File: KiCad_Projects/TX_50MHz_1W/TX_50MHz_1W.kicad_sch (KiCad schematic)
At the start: 38 parts, among them J1 AIL Stick, J10 I2C Exp / OLED, J11 ANT, J2 ELE Stick, J3 THR Stick, J4 RUD Stick, J5 AUX5, J6 AUX6, J7 AUX7, J8 V_BATT In (XT30), J9 5V Logic In, Q1 RD01MUS2 (1W PA), U1 ESP32-S3-WROOM-1-N16R8, U2 Si5351A-B-GT, U3 BGS12PL6 (T/R SW), U4 SPF5043Z (LNA), U5 LT5560 (Mixer), U6 ADS1115IDGSR (0x48), U7 ADS1115IDGSR (0x49), U8 SH1106 1.3in OLED, Y1 26.000MHz

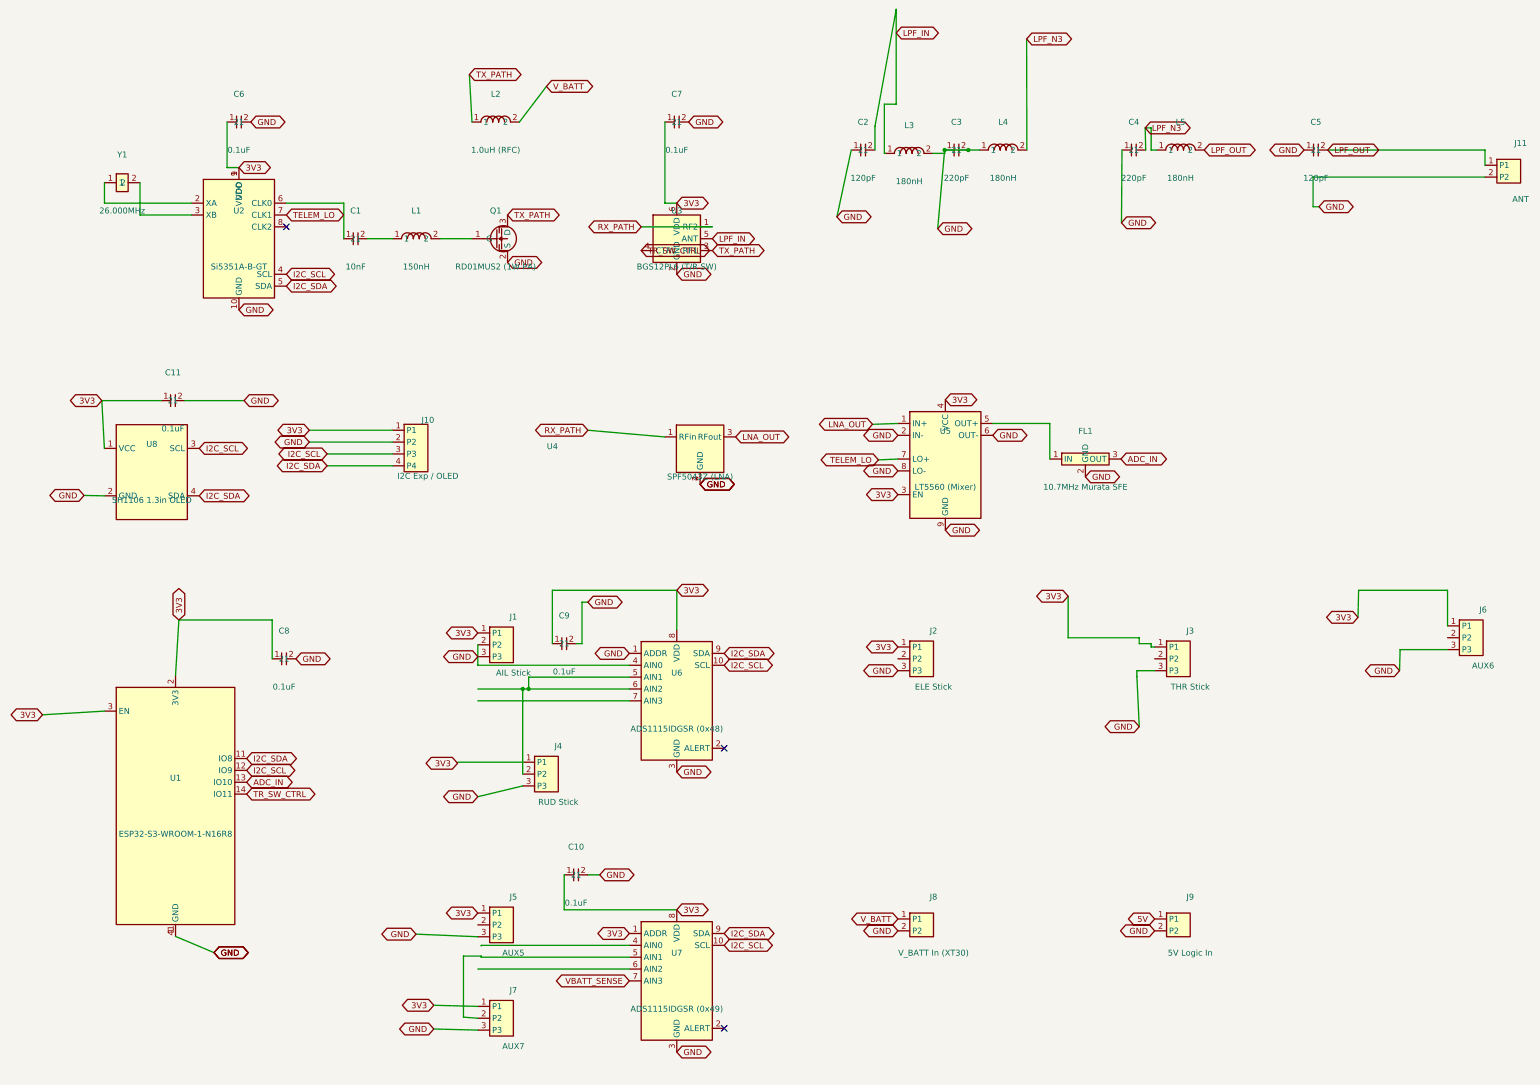
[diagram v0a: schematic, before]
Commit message: Grid-align symbols, wire the RF chain directly, use power symbols
Three related cosmetic/hygiene passes across both RX and TX schematics,
each verified with kicad-cli (netlist net-membership diff + ERC) to
confirm zero unintended connectivity change:

1. Grid alignment: every symbol placement had a small sub-grid
   fractional offset (not a multiple of the standard 1.27mm/50mil
   KiCad grid), making it impossible to snap new wires onto existing
   pins. Snapped every symbol to the nearest grid point and moved
   everything rigidly attached to it (labels, wire endpoints,
   junctions, no-connect markers) by the same delta.

2. Filter/amplifier direct wiring: the LNA -> mixer -> filter RF
   signal chain (SPF5043Z -> LT5560 -> 10.7MHz filter) used net
   labels to bridge components sitting a few centimeters apart on
   the same row. Replaced the label pairs with direct wires on both
   boards.

3. Power symbols: GND/3V3/5V/V_BATT were universally represented as
   text-shaped net labels (46-66% of all labels in each file) instead
   of KiCad's dedicated power symbols. Added power:GND/3V3/5V_RAIL/
   V_BATT/5V library symbols (GND copied byte-for-byte from KiCad's
   own power.kicad_sym; others follow the same template under
   project-specific names) and replaced every power-rail label with
   one, wired at the same point. This is also what real power symbols
   are for: ERC's "is this rail driven" check only recognizes them,
   not text labels.

The power symbol pass incidentally surfaced and fixed two pin
connections (TX: U7/C10's VDD net, and J4 pin 1) that were floating
by a fraction of a millimeter in the prior schematic - invisible at
any normal zoom, but not actually connected. Confirmed via netlist
diff that this was the only real connectivity change in either file;
everything else matches the prior net membership exactly.

Co-Authored-By: Claude Sonnet 5 <noreply@anthropic.com>
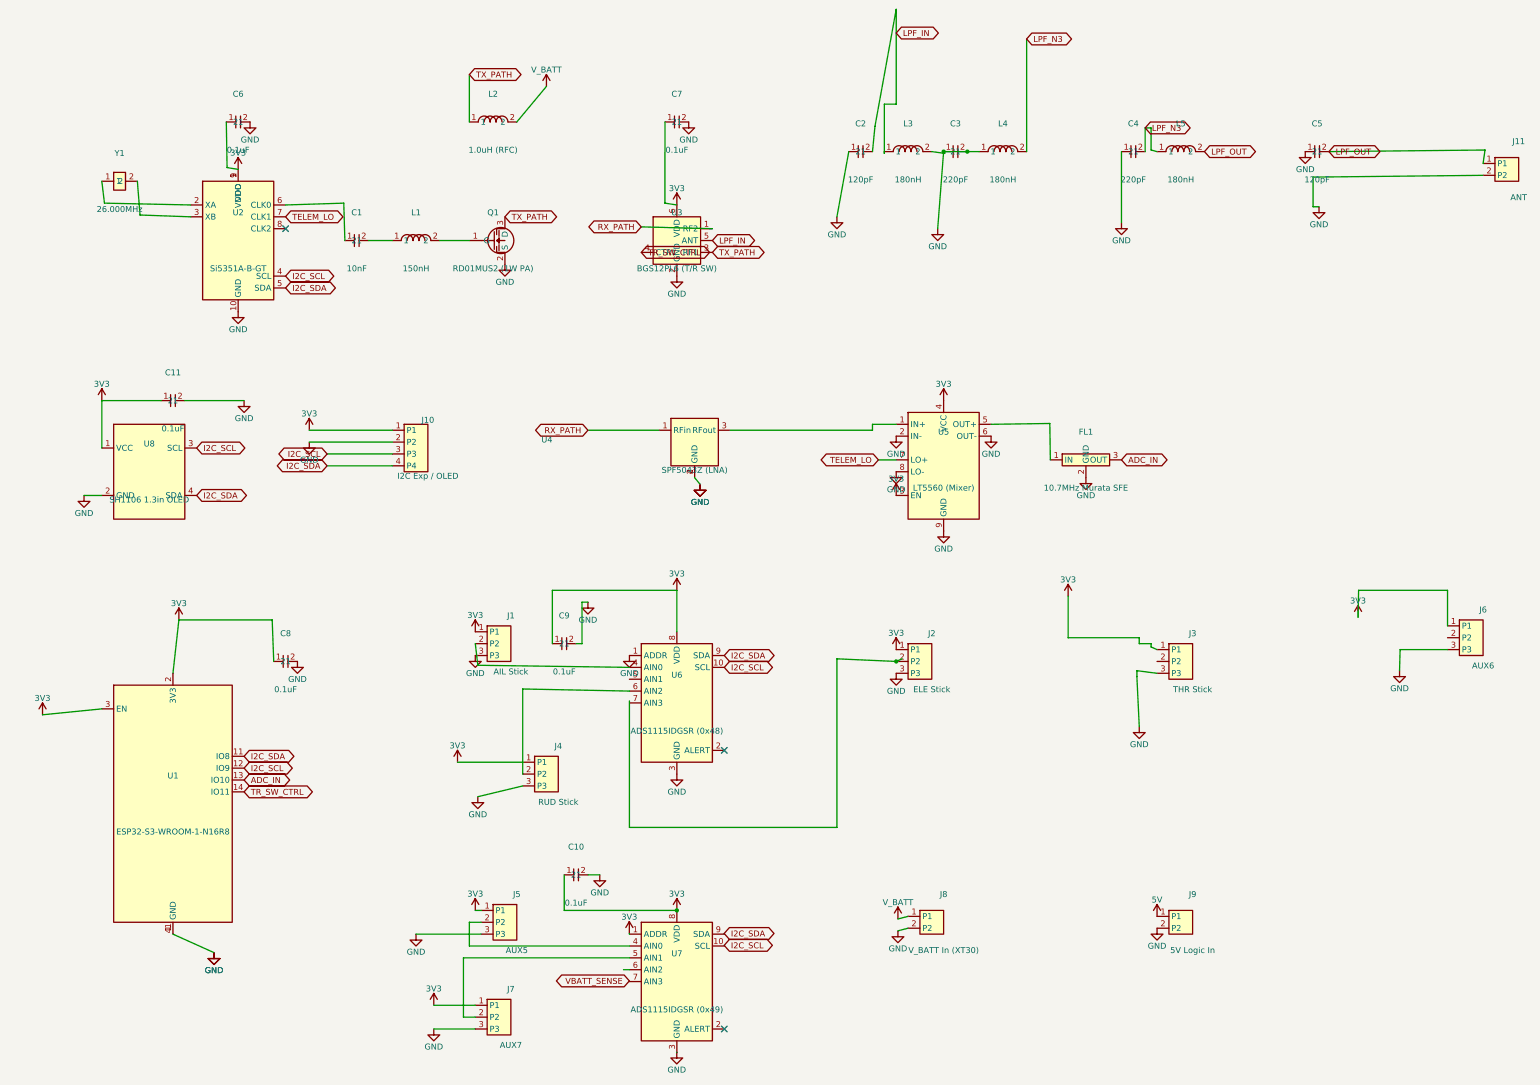
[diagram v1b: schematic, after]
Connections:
- net 3V3: now also J4.1 (P1)
- net GND: no longer J1.2 (P2), U6.4 (AIN0)
- net at U7.4 (AIN0): now also J5.2 (P2)
- net at J4.2 (P2), U6.6 (AIN2): no longer U6.5 (AIN1)
- net LNA_OUT: no longer names the net of U4.3 (RFout), U5.1 (IN+)
- new net: J1.2 (P2), U6.4 (AIN0)
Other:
- moved on the sheet: C2, C8, J1, J11, J2, J3, J5, J7, J8, J9, L2, Q1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

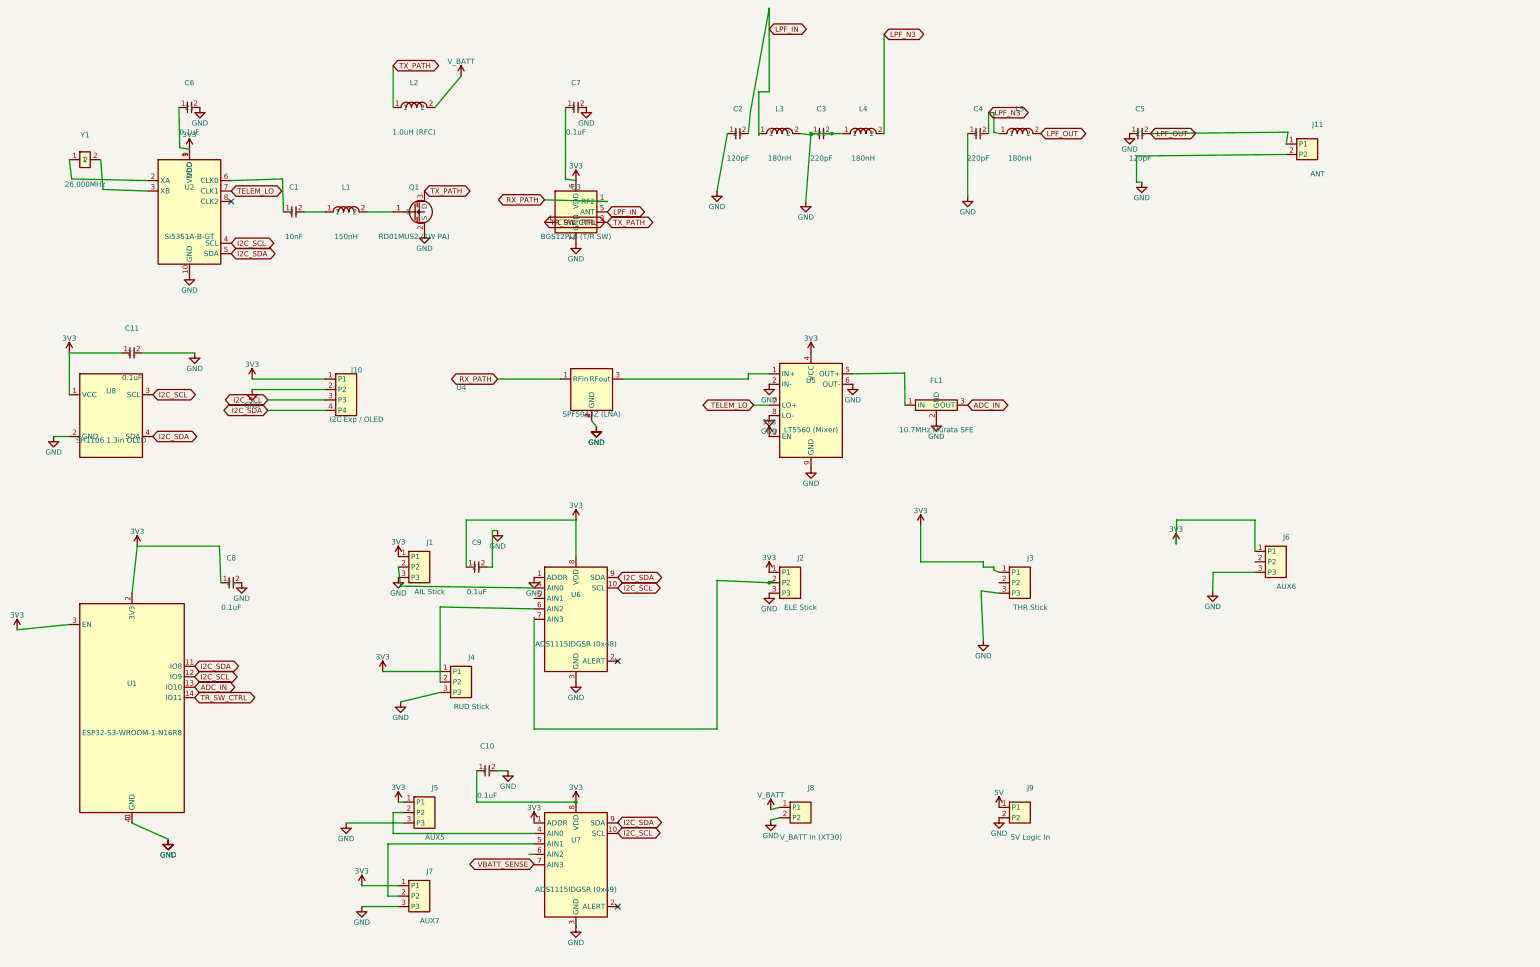
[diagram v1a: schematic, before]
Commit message: Update TX schematic/PCB and Kraft6M library (in-progress KiCad edits)
These files were modified outside this session (likely a parallel
KiCad GUI session on TX while RX work was in progress this
conversation) and are being committed as-is alongside the RX changes.
Includes a new TX_50MHz_1W.kicad_pcb. ERC sanity-checked clean load
before committing; content not otherwise reviewed by Claude.

Co-Authored-By: Claude Sonnet 5 <noreply@anthropic.com>
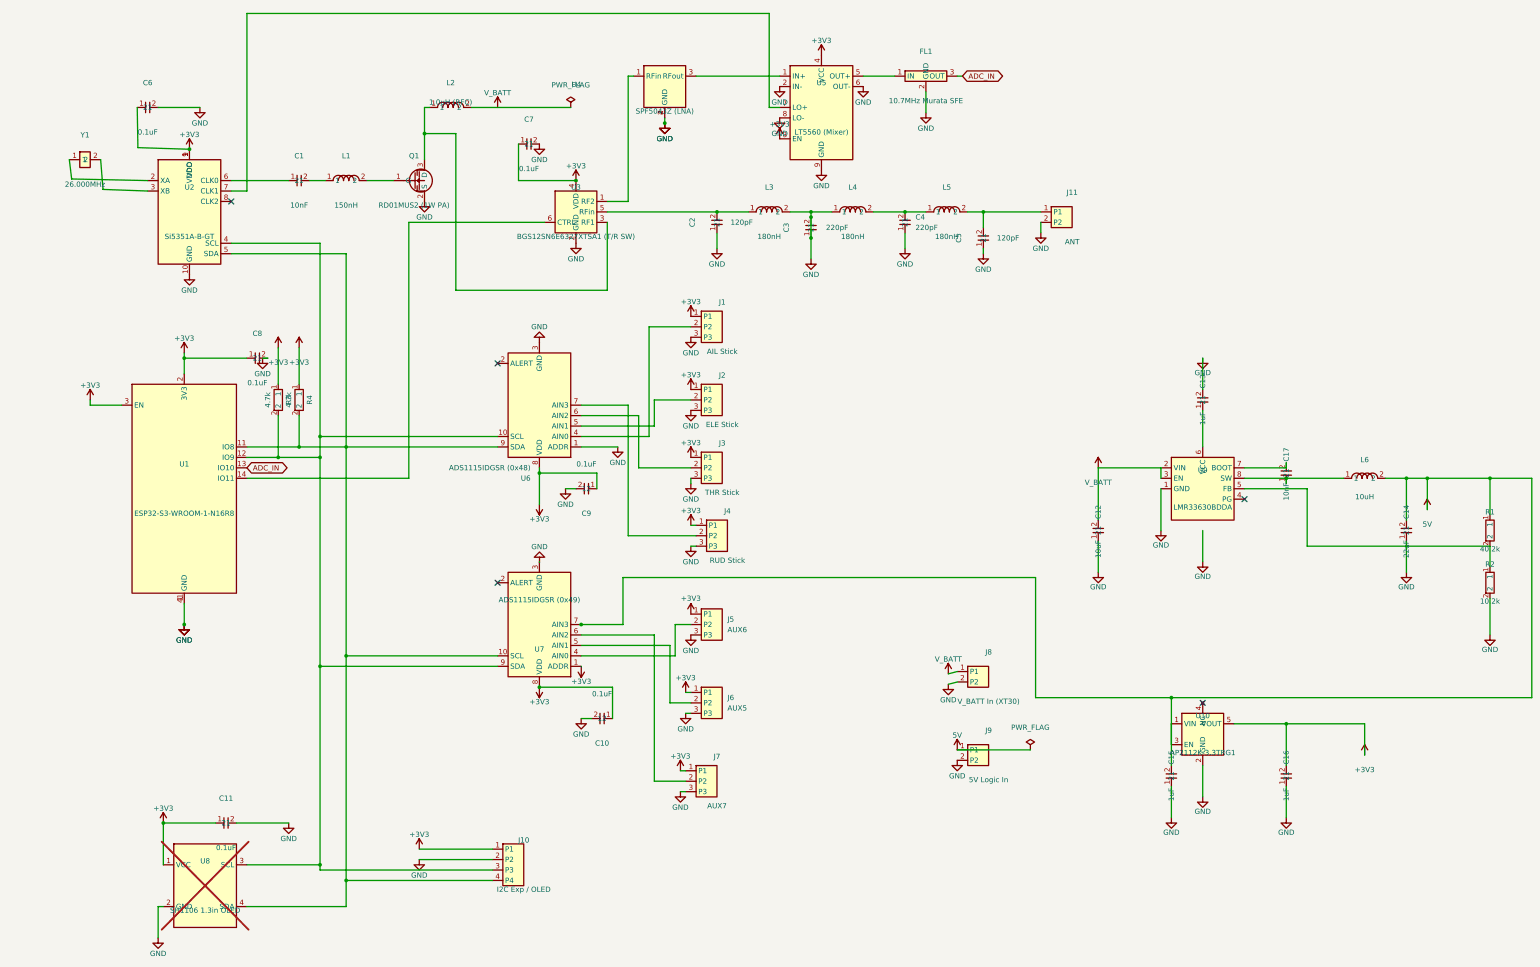
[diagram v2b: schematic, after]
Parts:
- added C12: 10uF, Capacitor_SMD:C_0805_2012Metric, symbol Kraft6M:C_10uF_0805
- added C13, C15, C16: 1uF, Capacitor_SMD:C_0603_1608Metric, symbol Kraft6M:C_1uF_0603
- added C14: 22uF, Capacitor_SMD:C_0805_2012Metric, symbol Kraft6M:C_22uF_0805
- added C17: 10nF, Capacitor_SMD:C_0603_1608Metric, symbol Kraft6M:C_10nF_0603
- added L6: 10uH, Inductor_SMD:L_0805_2012Metric, symbol Kraft6M:L_10uH_0805
- added R1: 40.2k, Resistor_SMD:R_0603_1608Metric, symbol Kraft6M:R_40.2k_0603
- added R2: 10.2k, Resistor_SMD:R_0603_1608Metric, symbol Kraft6M:R_10.2k_0603
- added R3, R4: 4.7k, Resistor_SMD:R_0603_1608Metric, symbol Kraft6M:R_4.7k_0603
- added U10: AP2112K-3.3TRG1, Package_TO_SOT_SMD:SOT-23-5, symbol Kraft6M:AP2112K-3.3
- added U9: LMR33630BDDA, Package_SO:Texas_HSOP-8-1EP_3.9x4.9mm_P1.27mm_ThermalVias, symbol Kraft6M:LMR33630
- FL1: footprint Filter:Ceramic_Filter_Murata_SFE -> Crystal:Resonator_SMD_Murata_SFECV-3Pin_6.9x2.9mm
- U1: footprint RF_Module:ESP32-S3-WROOM-1-N16R8 -> RF_Module:ESP32-S3-WROOM-1
- U3: value BGS12PL6 (T/R SW) -> BGS12SN6E6327XTSA1 (T/R SW); footprint Package_SON:TSLP-6-4_0.7x1.1mm_P0.4mm -> Package_LGA:Infineon_PG-TSNP-6-10_0.7x1.1mm_0.7x1.1mm_P0.4mm
- U5: footprint Package_SON:DFN-8-1EP_2x2mm_P0.5mm_EP0.6x1.0mm -> Package_DFN_QFN:DFN-8-1EP_2x2mm_P0.5mm_EP0.6x1.2mm
- U6, U7: footprint Package_SO:VSSOP-10_3x3mm_P0.5mm -> Package_SO:HVSSOP-10-1EP_3x3mm_P0.5mm_EP1.83x1.89mm
- U8: footprint Display:OLED-13-128x64 -> Connector_JST:JST_XH_B4B-XH-A_1x04_P2.50mm_Vertical; now not fitted
- renumbered J6 to J5, J5 to J6
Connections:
- net VBATT_SENSE is gone; now on net 5V: U7.7 (AIN3)
- net 5V: now also C14.2, C15.2, L6.2, R1.1, U10.1 (VIN), U10.3 (EN)
- net GND: now also C12.1, C13.2, C14.1, C15.1, C16.1, R2.2, U10.2 (GND), U9.1 (GND), U9.9 (GND)
- net V_BATT: now also C12.2, U9.2 (VIN), U9.3 (EN)
- net at J2.2 (P2): now also U6.5 (AIN1)
- net at J5.2 (P2): now also U7.4 (AIN0)
- net at J6.2 (P2): now also U7.5 (AIN1); no longer U7.4 (AIN0)
- net at J7.2 (P2): now also U7.6 (AIN2); no longer U7.5 (AIN1)
- net at U6.6 (AIN2): now also J3.2 (P2); no longer J4.2 (P2)
- net at U6.7 (AIN3): now also J4.2 (P2)
- net 3V3 renamed +3V3
- net +3V3: now also U3.4 (VDD), C16.2, R3.1, R4.1, U10.5 (VOUT); no longer U3.6 (VDD)
- net I2C_SCL: no longer names the net of J10.3 (P3), U1.12 (IO9), U2.4 (SCL), U6.10 (SCL), U8.3 (SCL)
- net I2C_SCL: now also U7.9 (SDA), R3.2; no longer U7.10 (SCL)
- net I2C_SDA: no longer names the net of J10.4 (P4), U1.11 (IO8), U2.5 (SDA), U6.9 (SDA), U8.4 (SDA)
- net I2C_SDA: now also U7.10 (SCL), R4.2; no longer U7.9 (SDA)
- net LPF_IN: no longer names the net of C2.2, L3.1, U3.5 (RFin)
- net LPF_N3: no longer names the net of C4.2, L4.2, L5.1
- net LPF_OUT: no longer names the net of C5.2, J11.1 (P1), L5.2
- net RX_PATH: no longer names the net of U3.1 (RF2), U4.1 (RFin)
- net TELEM_LO: no longer names the net of U2.7 (CLK1), U5.7 (LO+)
- net TR_SW_CTRL: no longer names the net of U1.14 (IO11)
- net TR_SW_CTRL: now also U3.6 (CTRL); no longer U3.4 (CTRL)
- net TX_PATH: no longer names the net of L2.1, Q1.3 (D), U3.3 (RF1)
- new net: R1.2, R2.1, U9.5 (FB)
- new net: C13.1, U9.6 (VCC)
- new net: C17.2, U9.7 (BOOT)
- new net: C17.1, L6.1, U9.8 (SW)
- no-connect marks 3 -> 5
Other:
- moved on the sheet: C1, C10, C11, C2, C3, C4, C5, C6, C7, C8, C9, FL1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

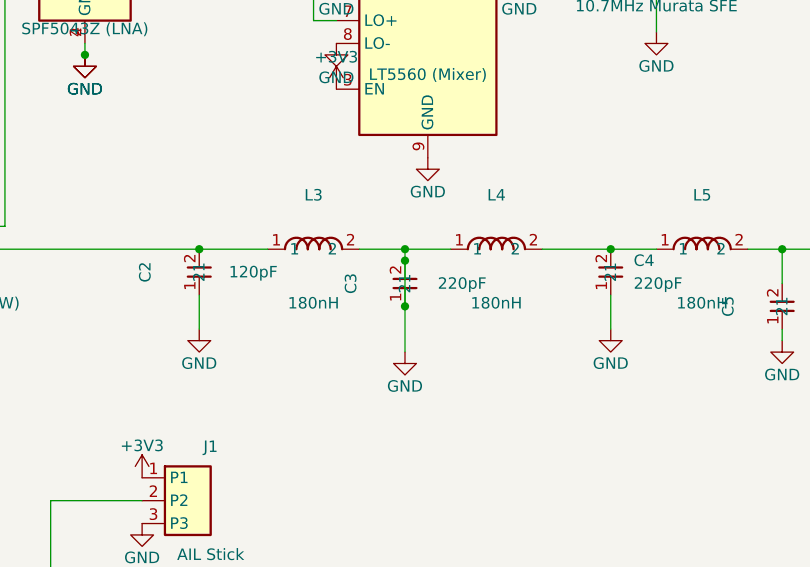
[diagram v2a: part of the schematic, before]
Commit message: Fix shorted C3 in TX antenna LPF, re-run S11/S21
Removed a stray wire in TX_50MHz_1W.kicad_sch that shorted C3's two
pads together and dragged the L3/L4 junction to GND. That short was
the actual cause of the earlier "disconnected antenna network" finding
-- with it removed, L3-C3-L4-C4-L5-C5 forms the complete 7-pole
low-pass filter the value pattern (120/220/220/120pF, 3x180nH) always
implied, running from the T/R switch common port to the antenna.

Re-simulated as a proper 2-port network: the filter now works (-67.6dB
rejection at the 100MHz 2nd harmonic), but the -3dB cutoff sits at
49.1MHz -- right on top of the 50MHz fundamental instead of safely
above it, so S21 is already down 5dB and S11 is poor (VSWR 10.4:1) at
the operating frequency. Flagged as a follow-up: rescale L/C values so
cutoff lands closer to 65-75MHz.

Co-Authored-By: Claude Sonnet 5 <noreply@anthropic.com>
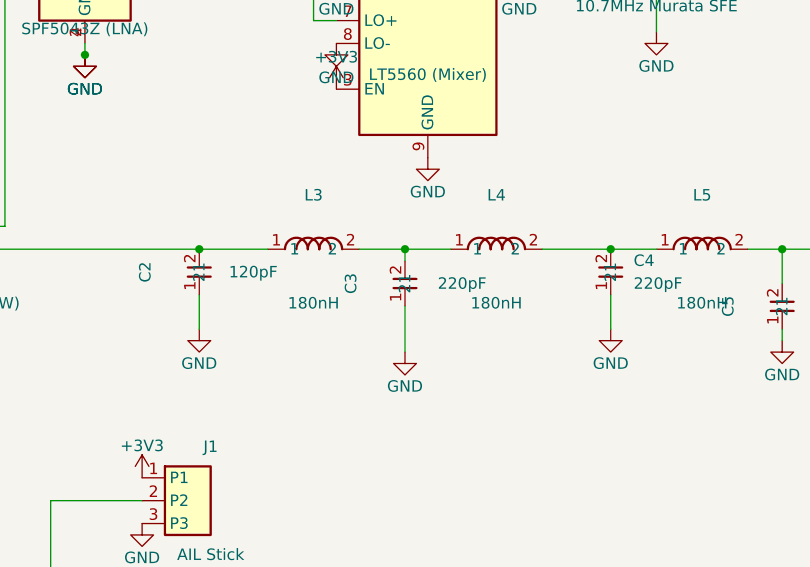
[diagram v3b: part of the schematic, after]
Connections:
- net GND: no longer C3.2, L3.2, L4.1
- new net: C3.2, L3.2, L4.1
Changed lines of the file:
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@@
-	)
-	(junction
-		(at 224.79 73.66)
-		(diameter 0)
-		(color 0 0 0 0)
 	)
 	(junction
@@
 	(junction
 		(at 105.41 182.88)
-		(diameter 0)
-		(color 0 0 0 0)
-	)
-	(junction
-		(at 224.79 78.74)
 		(diameter 0)
 		(color 0 0 0 0)
@@
 		)
 		(stroke
-			(width 0)
-			(type default)
-		)
-	)
-	(wire
-		(pts
-			(xy 224.79 78.74) (xy 224.79 73.66)
-		)
-		(stroke
